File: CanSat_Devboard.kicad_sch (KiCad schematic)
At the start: 0 parts

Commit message: Organized schematic pages
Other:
- sheet Power - Sequencing renamed LoRa
- sheet Project Architecture renamed SD card
- added sheet Misc (Misc.kicad_sch)
- added sheet OBC (OBC.kicad_sch)
- sheet LoRa: file Power - Sequencing.kicad_sch -> LoRa.kicad_sch
- sheet SD card: file Project Architecture.kicad_sch -> SD_card.kicad_sch
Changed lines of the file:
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@@
 			(color 0 0 0 0)
 		)
-		(property "Sheetname" "Power - Sequencing"
+		(property "Sheetname" "LoRa"
 			(at 340.36 312.6609 0)
 			(show_name no)
@@
 			)
 		)
-		(property "Sheetfile" "Power - Sequencing.kicad_sch"
+		(property "Sheetfile" "LoRa.kicad_sch"
 			(at 341.63 314.96 0)
 			(show_name no)
@@
 			(project "CanSat_Devboard"
 				(path "/f9e05184-c88b-4a88-ae9c-ab2bdb32be7c"
-					(page "6")
+					(page "5")
+				)
+			)
+		)
+	)
+	(sheet
+		(at 340.36 323.85)
+		(size 35.56 5.08)
+		(exclude_from_sim no)
+		(in_bom yes)
+		(on_board yes)
+		(dnp no)
+		(stroke
+			(width 0.1524)
+			(type solid)
+		)
+		(fill
+			(color 0 0 0 0)
+		)
+		(property "Sheetname" "OBC"
+			(at 340.36 322.834 0)
+			(show_name no)
+			(do_not_autoplace no)
+			(effects
+				(font
+					(face "Times New Roman")
+					(size 1.905 1.905)
+					(bold yes)
+					(color 0 0 0 1)
+				)
+				(justify left bottom)
+			)
+		)
+		(property "Sheetfile" "OBC.kicad_sch"
+			(at 341.63 325.12 0)
+			(show_name no)
+			(do_not_autoplace no)
+			(effects
+				(font
+					(face "Arial")
+					(size 1.27 1.27)
+				)
+				(justify left top)
+			)
+		)
+		(instances
+			(project "CanSat_Devboard"
+				(path "/f9e05184-c88b-4a88-ae9c-ab2bdb32be7c"
+					(page "4")
 				)
 			)
@@
 			(project "CanSat_Devboard"
 				(path "/f9e05184-c88b-4a88-ae9c-ab2bdb32be7c"
+					(page "3")
+				)
+			)
+		)
+	)
+	(sheet
+		(at 299.72 323.85)
+		(size 35.56 5.08)
+		(exclude_from_sim no)
+		(in_bom yes)
+		(on_board yes)
+		(dnp no)
+		(stroke
+			(width 0.1524)
+			(type solid)
+		)
+		(fill
+			(color 0 0 0 0)
+		)
+		(property "Sheetname" "Misc"
+			(at 299.72 322.8209 0)
+			(show_name no)
+			(do_not_autoplace no)
+			(effects
+				(font
+					(size 1.905 1.905)
+					(thickness 0.381)
+					(bold yes)
+					(color 0 0 0 1)
+				)
+				(justify left bottom)
+			)
+		)
+		(property "Sheetfile" "Misc.kicad_sch"
+			(at 300.482 324.866 0)
+			(show_name no)
+			(do_not_autoplace no)
+			(effects
+				(font
+					(size 1.27 1.27)
+				)
+				(justify left top)
+			)
+		)
+		(instances
+			(project "CanSat_Devboard"
+				(path "/f9e05184-c88b-4a88-ae9c-ab2bdb32be7c"
 					(page "7")
 				)
@@
 			(color 0 0 0 0)
 		)
-		(property "Sheetname" "Project Architecture"
-			(at 299.72 312.6609 0)
-			(show_name no)
-			(do_not_autoplace no)
-			(effects
-				(font
-					(face "Times New Roman")
-					(size 1.905 1.905)
-					(bold yes)
-					(color 0 0 0 1)
-				)
-				(justify left bottom)
-			)
-		)
-		(property "Sheetfile" "Project Architecture.kicad_sch"
+		(property "Sheetname" "SD card"
+			(at 299.72 312.674 0)
+			(show_name no)
+			(do_not_autoplace no)
+			(effects
+				(font
+					(face "Times New Roman")
+					(size 1.905 1.905)
+					(bold yes)
+					(color 0 0 0 1)
+				)
+				(justify left bottom)
+			)
+		)
+		(property "Sheetfile" "SD_card.kicad_sch"
 			(at 300.99 314.96 0)
 			(show_name no)
@@
 			(project "CanSat_Devboard"
 				(path "/f9e05184-c88b-4a88-ae9c-ab2bdb32be7c"
-					(page "3")
-				)
-			)
+					(page "6")
+				)
+			)

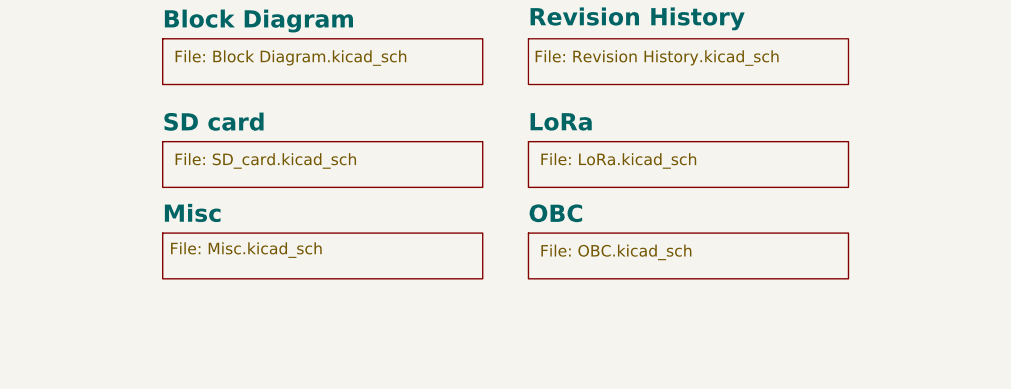
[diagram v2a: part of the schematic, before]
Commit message: Pasted schematics from previous design
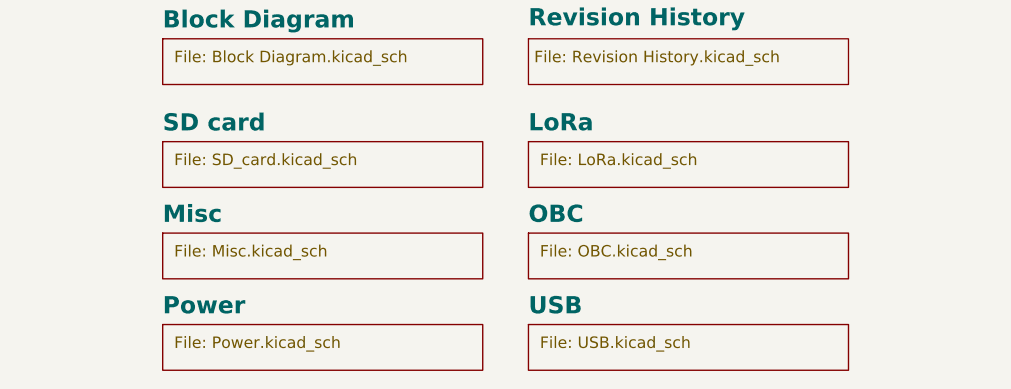
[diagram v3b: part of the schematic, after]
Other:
- added sheet Power (Power.kicad_sch)
- added sheet USB (USB.kicad_sch)
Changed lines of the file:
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@@
+	)
+	(sheet
+		(at 299.72 334.01)
+		(size 35.56 5.08)
+		(exclude_from_sim no)
+		(in_bom yes)
+		(on_board yes)
+		(dnp no)
+		(stroke
+			(width 0.1524)
+			(type solid)
+		)
+		(fill
+			(color 0 0 0 0)
+		)
+		(property "Sheetname" "Power"
+			(at 299.72 332.994 0)
+			(show_name no)
+			(do_not_autoplace no)
+			(effects
+				(font
+					(face "Times New Roman")
+					(size 1.905 1.905)
+					(bold yes)
+					(color 0 0 0 1)
+				)
+				(justify left bottom)
+			)
+		)
+		(property "Sheetfile" "Power.kicad_sch"
+			(at 300.99 335.28 0)
+			(show_name no)
+			(do_not_autoplace no)
+			(effects
+				(font
+					(face "Arial")
+					(size 1.27 1.27)
+				)
+				(justify left top)
+			)
+		)
+		(instances
+			(project "CanSat_Devboard"
+				(path "/f9e05184-c88b-4a88-ae9c-ab2bdb32be7c"
+					(page "8")
+				)
+			)
+		)
+	)
+	(sheet
+		(at 299.72 323.85)
+		(size 35.56 5.08)
+		(exclude_from_sim no)
+		(in_bom yes)
+		(on_board yes)
+		(dnp no)
+		(stroke
+			(width 0.1524)
+			(type solid)
+		)
+		(fill
+			(color 0 0 0 0)
+		)
+		(property "Sheetname" "Misc"
+			(at 299.72 322.834 0)
+			(show_name no)
+			(do_not_autoplace no)
+			(effects
+				(font
+					(face "Times New Roman")
+					(size 1.905 1.905)
+					(bold yes)
+					(color 0 0 0 1)
+				)
+				(justify left bottom)
+			)
+		)
+		(property "Sheetfile" "Misc.kicad_sch"
+			(at 300.99 325.12 0)
+			(show_name no)
+			(do_not_autoplace no)
+			(effects
+				(font
+					(face "Arial")
+					(size 1.27 1.27)
+				)
+				(justify left top)
+			)
+		)
+		(instances
+			(project "CanSat_Devboard"
+				(path "/f9e05184-c88b-4a88-ae9c-ab2bdb32be7c"
+					(page "7")
+				)
+			)
+		)
 	)
 	(sheet
@@
 	)
 	(sheet
-		(at 299.72 323.85)
-		(size 35.56 5.08)
-		(exclude_from_sim no)
-		(in_bom yes)
-		(on_board yes)
-		(dnp no)
-		(stroke
-			(width 0.1524)
-			(type solid)
-		)
-		(fill
-			(color 0 0 0 0)
-		)
-		(property "Sheetname" "Misc"
-			(at 299.72 322.8209 0)
-			(show_name no)
-			(do_not_autoplace no)
-			(effects
-				(font
-					(size 1.905 1.905)
-					(thickness 0.381)
-					(bold yes)
-					(color 0 0 0 1)
-				)
-				(justify left bottom)
-			)
-		)
-		(property "Sheetfile" "Misc.kicad_sch"
-			(at 300.482 324.866 0)
-			(show_name no)
-			(do_not_autoplace no)
-			(effects
-				(font
-					(size 1.27 1.27)
-				)
-				(justify left top)
-			)
-		)
-		(instances
-			(project "CanSat_Devboard"
-				(path "/f9e05184-c88b-4a88-ae9c-ab2bdb32be7c"
-					(page "7")
-				)
-			)
-		)
-	)
-	(sheet
 		(at 299.72 302.26)
 		(size 35.56 5.08)
@@
 				)
 			)
+		)
+	)
+	(sheet
+		(at 340.36 334.01)
+		(size 35.56 5.08)
+		(exclude_from_sim no)
+		(in_bom yes)
+		(on_board yes)
+		(dnp no)
+		(stroke
+			(width 0.1524)
+			(type solid)
+		)
+		(fill
+			(color 0 0 0 0)
+		)
+		(property "Sheetname" "USB"
+			(at 340.36 332.994 0)
+			(show_name no)
+			(do_not_autoplace no)
+			(effects
+				(font
+					(face "Times New Roman")
+					(size 1.905 1.905)
+					(bold yes)
+					(color 0 0 0 1)
+				)
+				(justify left bottom)
+			)
+		)
+		(property "Sheetfile" "USB.kicad_sch"
+			(at 341.63 335.28 0)
+			(show_name no)
+			(do_not_autoplace no)
+			(effects
+				(font
+					(face "Arial")
+					(size 1.27 1.27)
+				)
+				(justify left top)
+			)
+		)
+		(instances
+			(project "CanSat_Devboard"
+				(path "/f9e05184-c88b-4a88-ae9c-ab2bdb32be7c"
+					(page "9")
+				)
+			)

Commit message: Changed a few preferences
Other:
- note added: "Variant: ${VERSION}"
- note removed: "Variant: ${VARIANT}"
- title: (none) -> CanSat devboard
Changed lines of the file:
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@@
 	(paper "A3")
 	(title_block
-		(date "2025-01-12")
+		(title "CanSat devboard")
+		(date "2026-07-05")
 		(rev "${REVISION}")
 		(company "${COMPANY}")
 	)
-	(text "Variant: ${VARIANT}"
+	(text "Variant: ${VERSION}"
 		(exclude_from_sim no)
 		(at 25.4 58.42 0)

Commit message: Finished preliminary project schematics and architecture
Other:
- removed sheet LoRa
- removed sheet Misc
- removed sheet OBC
- removed sheet Power
- removed sheet SD card
- removed sheet USB
- added sheet Project Architecture (Project Architecture.kicad_sch)
